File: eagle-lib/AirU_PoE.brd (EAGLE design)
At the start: 71.1 x 79.5 mm, 111 parts, among them J8 SI-52003-F, Q1 BSS138W-7-F, Q2 MMBT3904LT1G, Q3 MMBT3904LT1G, Q5 NCE3407A, U1 HDC1080DMBT, U10 ENC28J60ENC28J60-I/SS0P, U13 AG9900M, U2 CH340T-SSOP20, U3 CJT1117-3.3-SOT223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

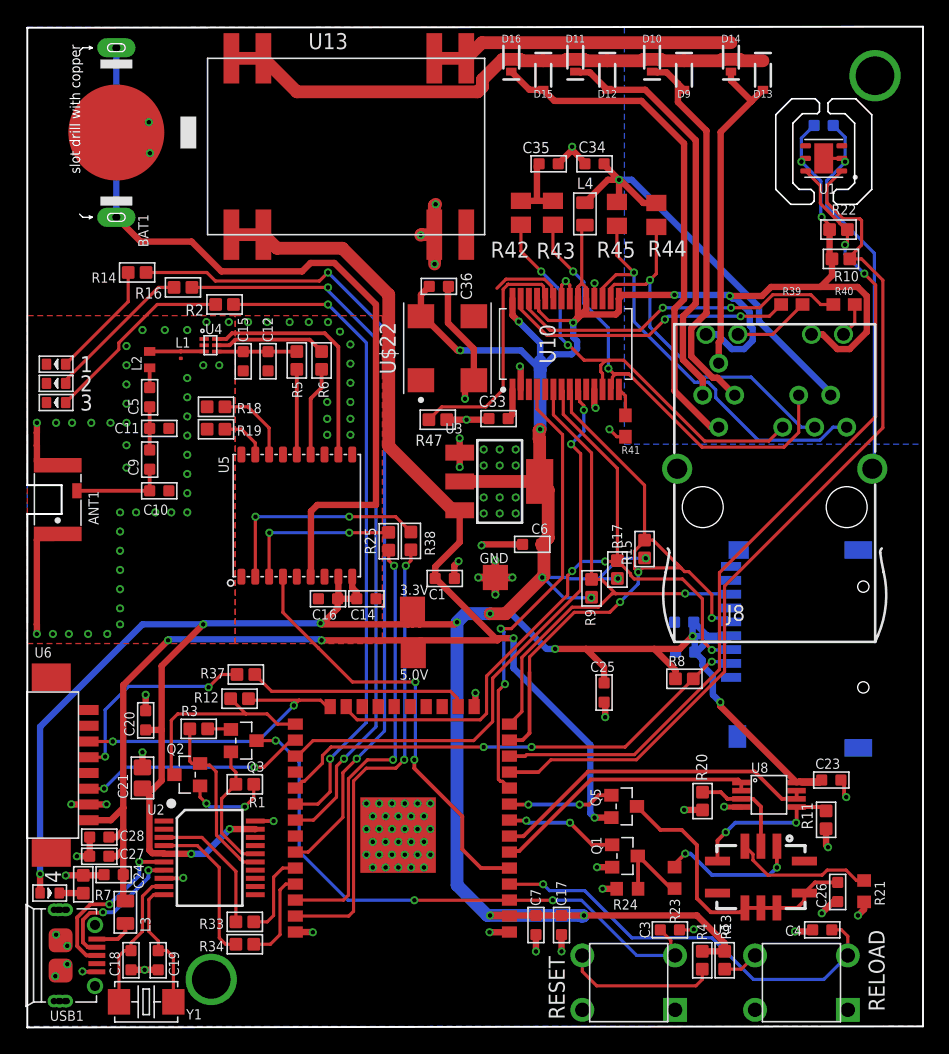
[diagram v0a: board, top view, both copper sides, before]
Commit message: Added PoE components
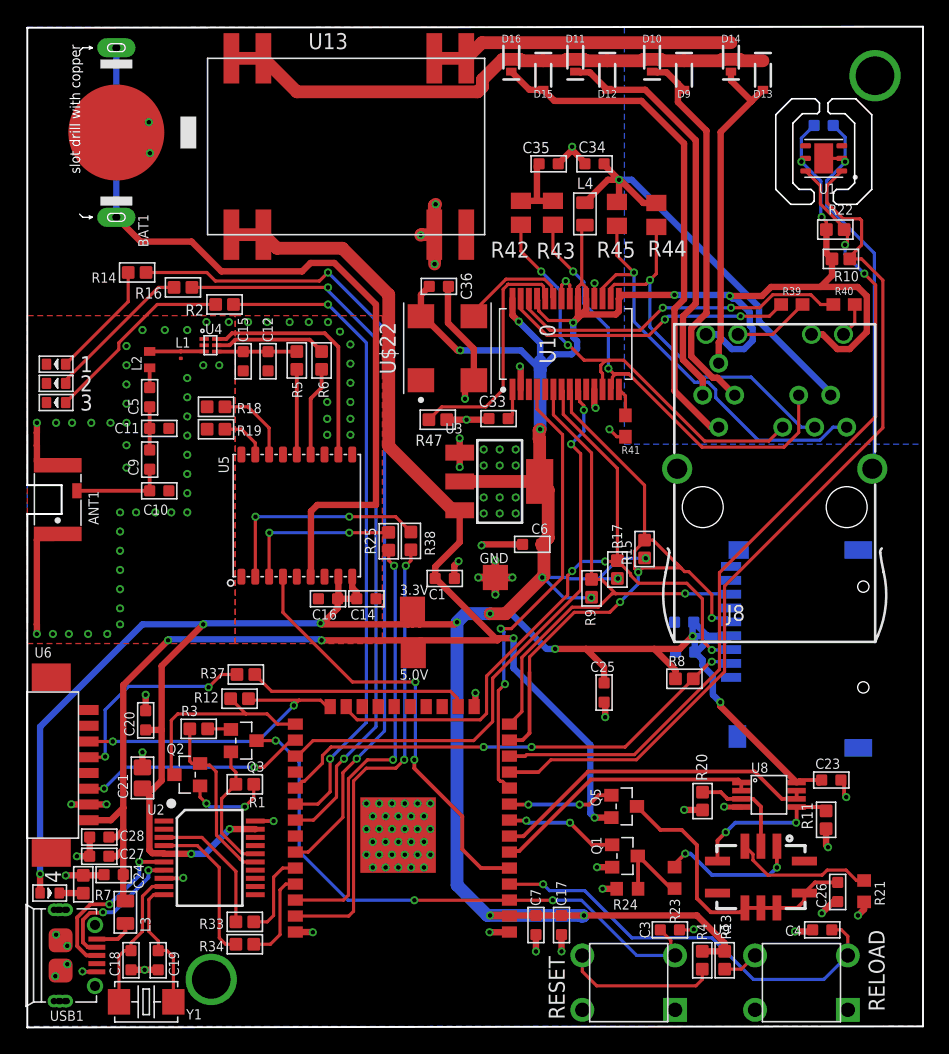
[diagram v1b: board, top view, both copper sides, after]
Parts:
- moved R22 0.25 mm to (64.2, 63.3)
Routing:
- net ETH_OSC1: track 5.92 -> 8.90 mm
- net 3.3V: track 352.7 -> 351.3 mm
- net VCAP: track 2.97 -> 2.46 mm

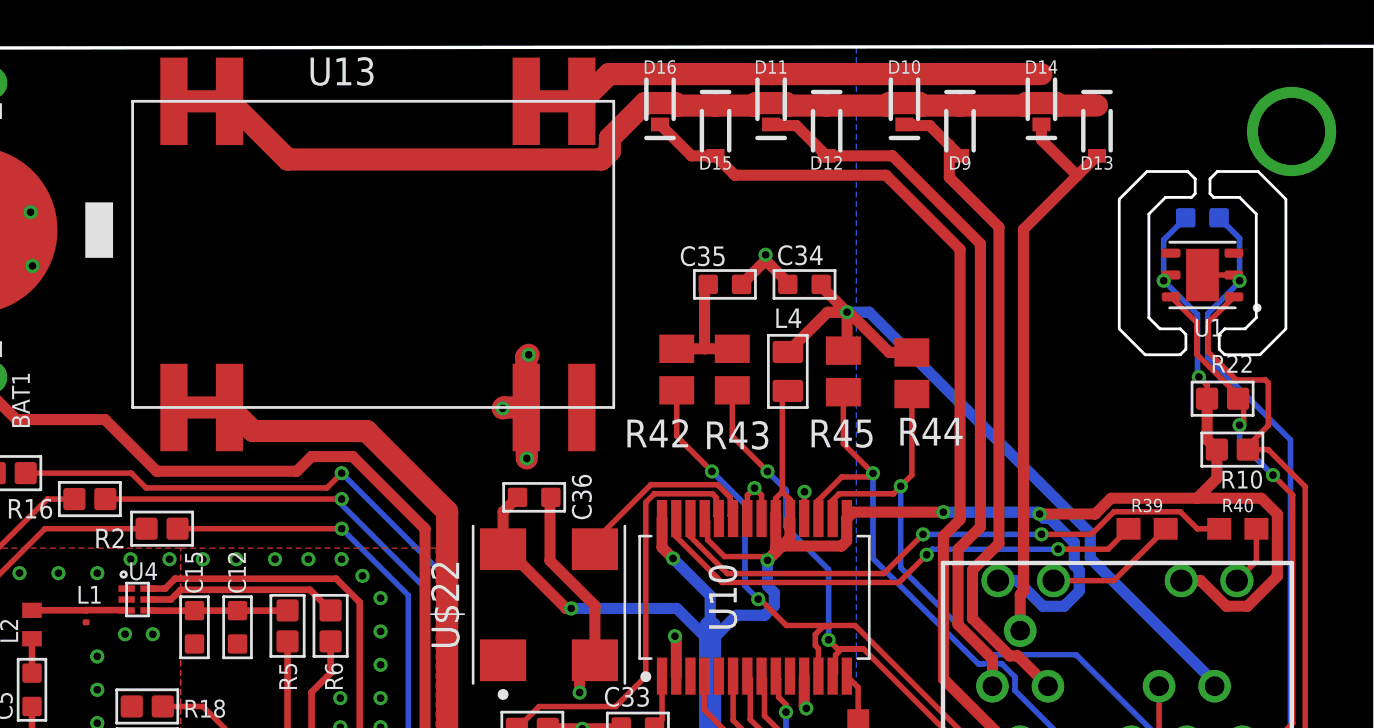
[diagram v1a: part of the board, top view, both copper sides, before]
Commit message: fixed AG9900M pins
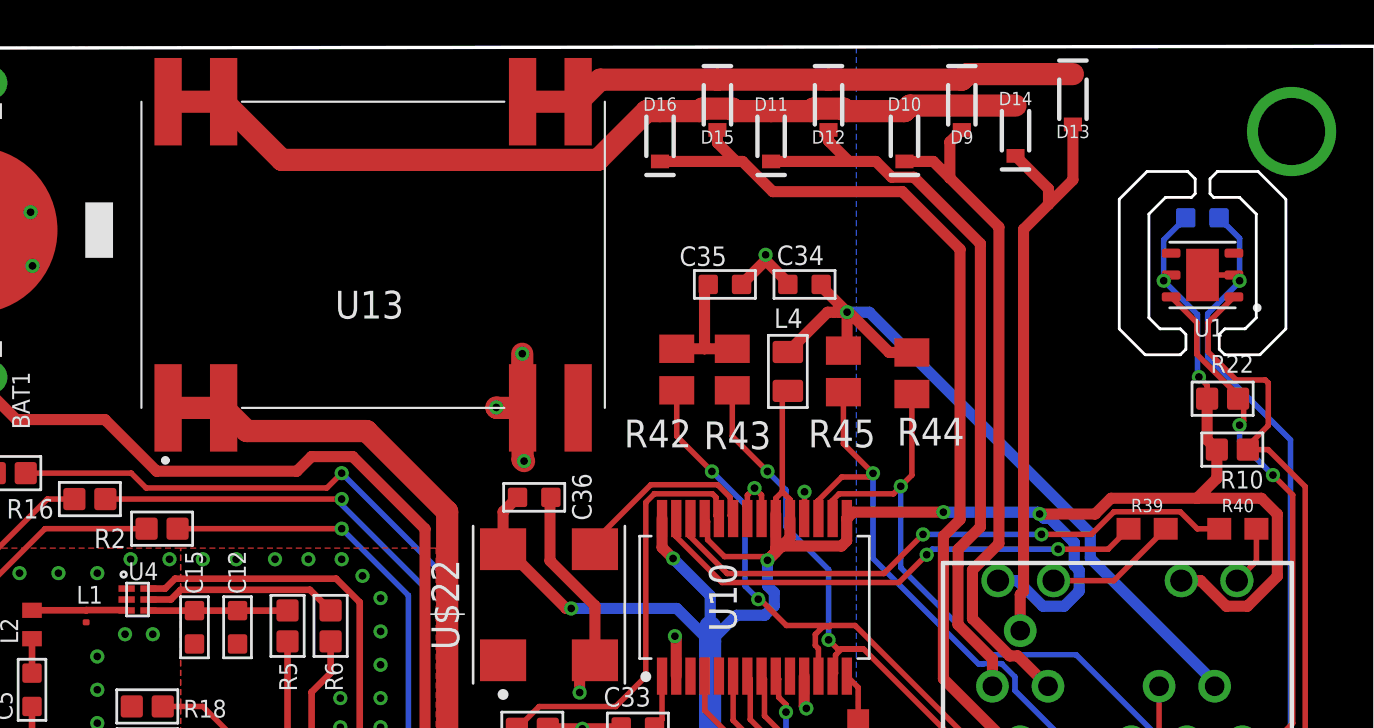
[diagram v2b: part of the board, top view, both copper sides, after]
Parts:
- U13: device AG9900M:AG9900M/MT -> Ag9900M:AG9900M
- moved D14 1.86 mm to (54.7, 75.6)
- moved D13 1.81 mm to (57.3, 77.0)
- moved D10 1.69 mm to (49.6, 75.3)
- moved D11 1.69 mm to (43.5, 75.3)
- moved D16 1.69 mm to (38.4, 75.3)
- moved D12 1.19 mm to (46.1, 76.8)
- moved D15 1.19 mm to (41.1, 76.8)
- moved D9 1.19 mm to (52.2, 76.8)
- moved U13 1.02 mm to (25.3, 69.9)
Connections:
- net 5.0V: now also U13.1, U13.2; no longer U13.P$6, U13.P$7
- net GND: now also U13.3; no longer U13.P$5
- net POE_VIN+: now also U13.5, U13.6; no longer U13.P$2, U13.P$3
- net POE_VIN-: now also U13.7, U13.8; no longer U13.P$1, U13.P$4
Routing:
- net POE_VIN+: track 45.1 -> 25.7 mm
- net POE_VIN-: track 24.1 -> 41.1 mm
- net ETH_VC2+: track 33.1 -> 34.3 mm
- net ETH_VC1-: track 40.7 -> 41.8 mm
- net ETH_VC2-: track 26.2 -> 27.0 mm
